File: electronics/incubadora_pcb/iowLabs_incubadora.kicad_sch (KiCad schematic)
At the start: 61 parts, among them J1 HDR-4x1, J10 HDR-4x1, J11 Conn_02x04_Odd_Even, J12 Conn_02x04_Odd_Even, J13 HDR-2x1, J2 VIN, J3 ON OFF, J4 HDR-2x1, J5 HDR-4x1, J6 HDR-5x1, J7 HDR-4x1, J8 HDR-4x1, J9 HDR-2x1, P1 USB_C_Plug_USB2.0, Q2 Q_PMOS_GSD, SW1 SW_DIP_x02, SW2 SW_DIP_x02, U3 ESP32-S3-WROOM-1, U5 XL4015, U6 LM1117MP-3.3

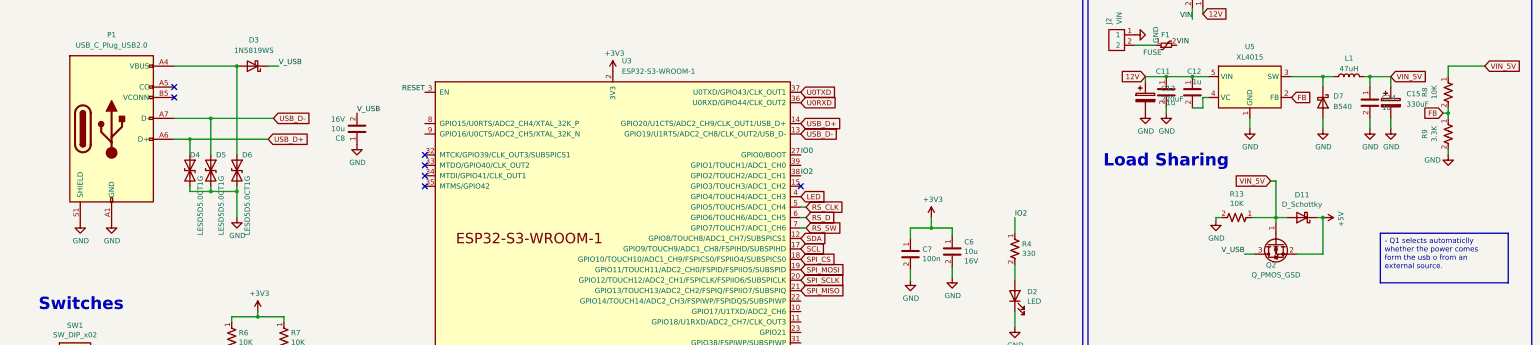
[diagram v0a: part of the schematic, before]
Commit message: updating 3d model of pcb
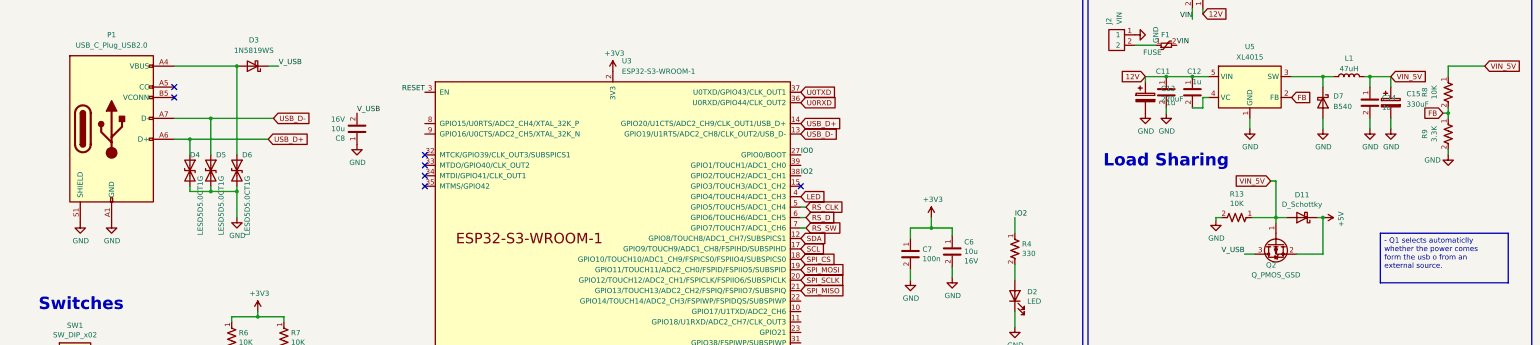
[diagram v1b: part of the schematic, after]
